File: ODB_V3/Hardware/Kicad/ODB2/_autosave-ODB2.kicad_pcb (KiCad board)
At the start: 6 copper layers, 63.1 x 114.6 mm, 243 parts, among them IC1 W25Q512JVEIQ, J1 Screw_Terminal_01x08, J11 Conn_02x04_Odd_Even, J15 Vin_XT30PW-F, J2 RFD_GT17HN-4DP-2HA56, J3 SYS_SW_Conn_01x05_Header, J4 142-0701-801, J5 MEM2067, J6 IdeFIX_GT17HN-4DP-2HA56, U1 STM32F412ZGTx, U10 ADXL382-2BCCZ-RL7, U11 SI5442DU-T1-GE3, U12 SI5442DU-T1-GE3, U13 L6981N33DR, U2 LM339, U3 SI5442DU-T1-GE3, U4 MS561101BA03-50, U5 L76L-M33, U6 BNO055, U7 MPQ9843GLE-5-AEC1-Z, U8 SI5442DU-T1-GE3, U9 MAX6612MXK, Y1 ABM8G-25.000MHZ-18-D2Y-T

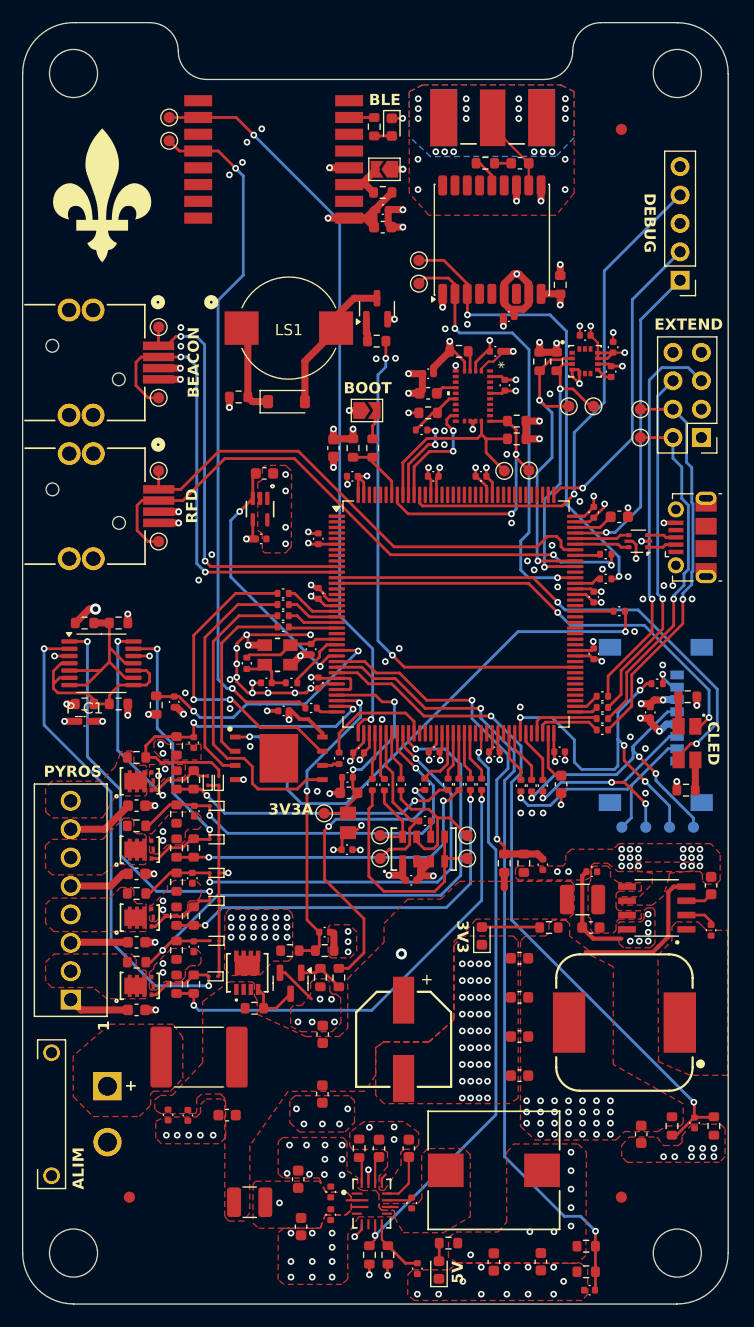
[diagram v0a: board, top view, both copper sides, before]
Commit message: wip : reduce BOM size to 50 SMD components
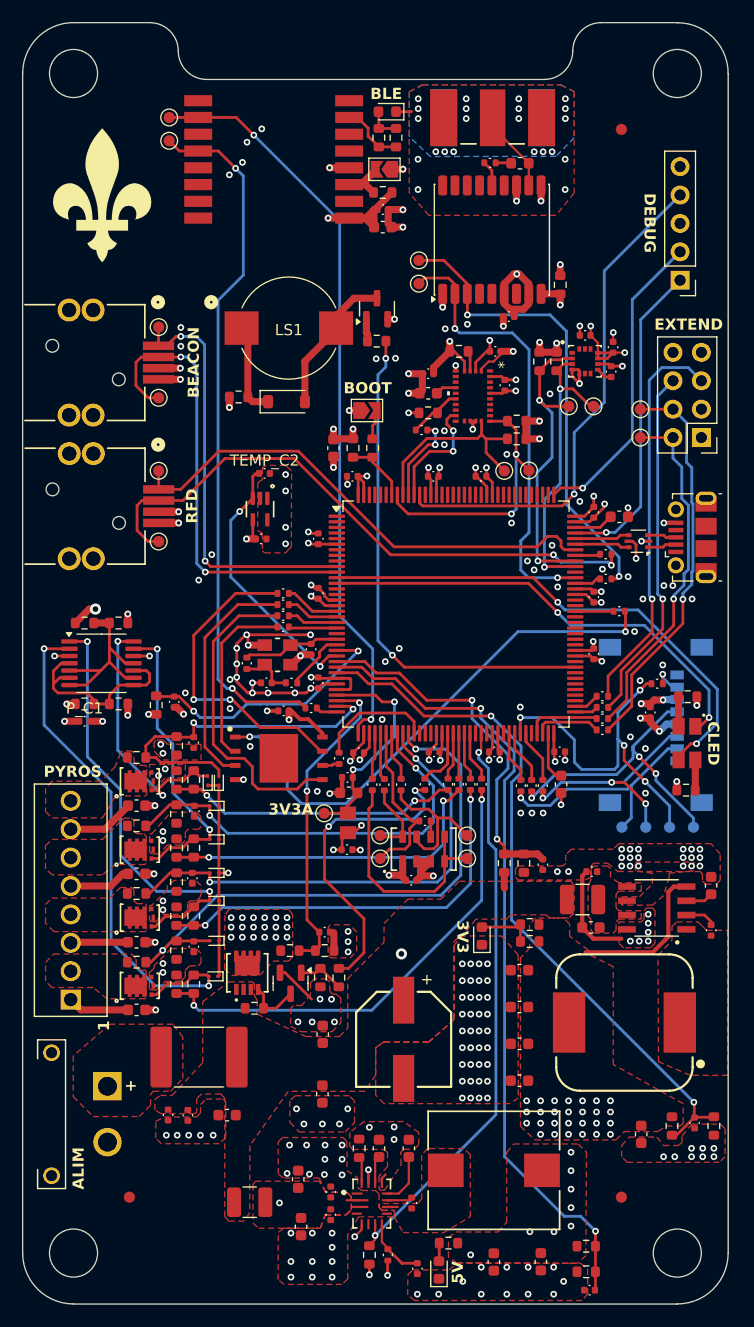
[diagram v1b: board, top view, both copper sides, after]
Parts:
- added 3V3_R4: 1.5k, Resistor_SMD:R_0603_1608Metric, F.Cu at (162.8, 123.6)
- added BT_R4: 1.5k, Resistor_SMD:R_0603_1608Metric, F.Cu at (150.8, 51.7)
- 3V3_R3: value 100R -> 1.5k
- 5V_R2, L76L_R1: footprint Resistor_SMD:R_0603_1608Metric -> ODB:R_0402_1005Metric
- BT_LED1: value BLUE -> GREEN
- Crystal_R1: value 0R -> 10R
- TEMP_C2: value 1nF -> 10nF; footprint Capacitor_SMD:C_0603_1608Metric -> ODB:C_0402_1005Metric
- moved 3V3_R3 1.74 mm to (162.8, 122.1)
- moved BT_LED1 1.44 mm to (150.1, 49.4), turned to 180 degrees
- moved 3V3_C7 1.06 mm to (161.9, 126.2)
- moved BT_R2 1.06 mm to (149.3, 51.7), turned to 90 degrees
- moved 3V3_C6 0.86 mm to (161.9, 129.5)
- moved 3V3_C5 0.66 mm to (161.9, 132.8)
- moved 3V3_C8 0.45 mm to (161.9, 136.1)
- moved L76L_R1 0.42 mm to (159.2, 54.0)
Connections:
- J5 pad 4: 3V3_Main -> unconnected-(J5-VDD-Pad4)
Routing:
- net Net-(H5-PIO1): track 2.25 -> 5.71 mm
- net Net-(BT_LED1-A): track 1.58 -> 3.05 mm
- net GND: track 139.3 -> 139.7 mm, vias 274 -> 273
